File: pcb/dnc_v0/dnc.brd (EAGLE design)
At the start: 100 x 80 mm, 1 part

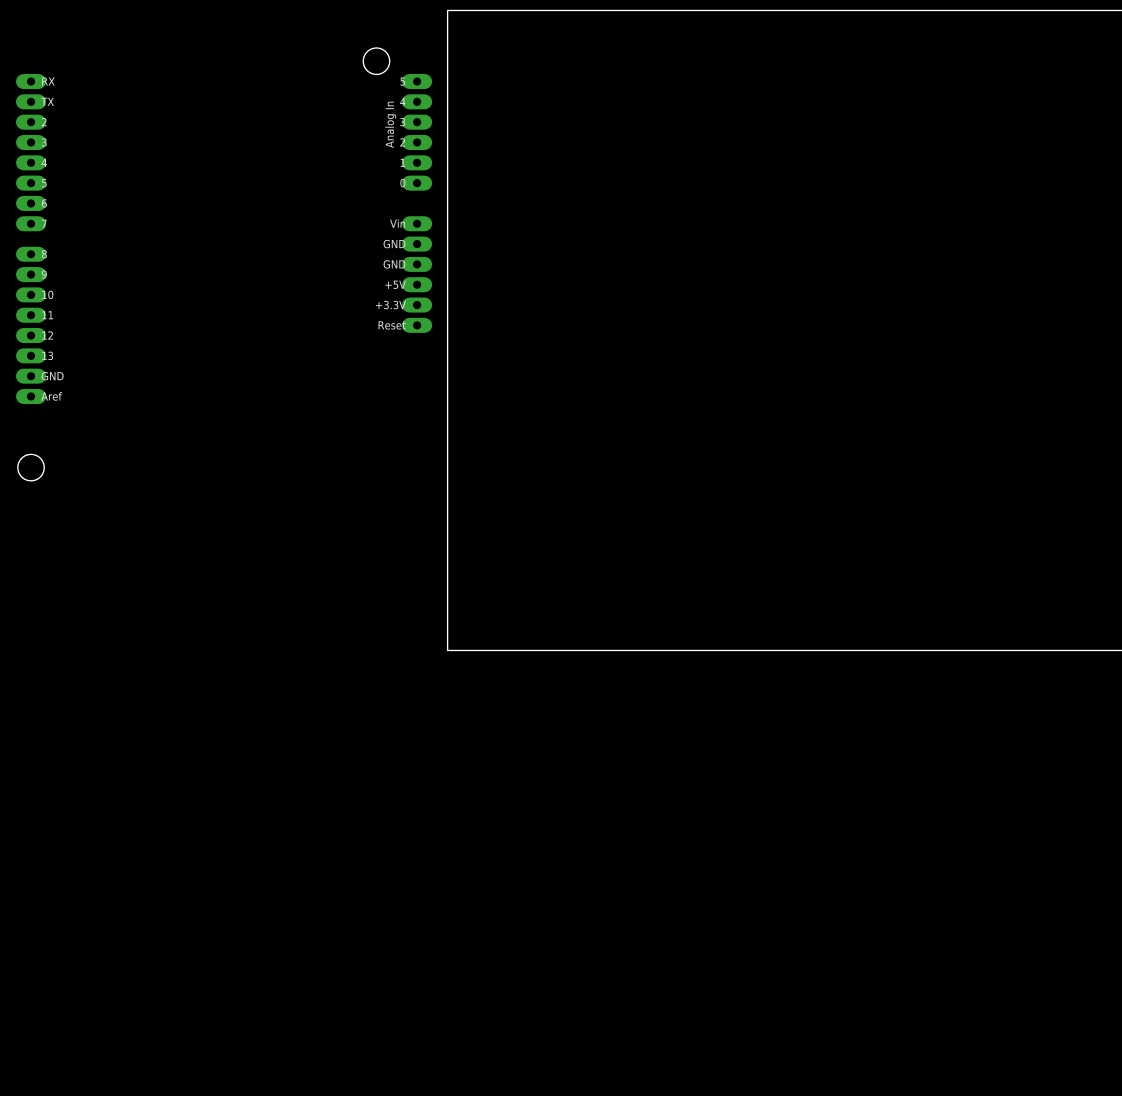
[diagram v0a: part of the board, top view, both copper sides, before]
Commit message: draw yunshield eagle-objet in a eaglelib pcb add sunshield eagle file in docref
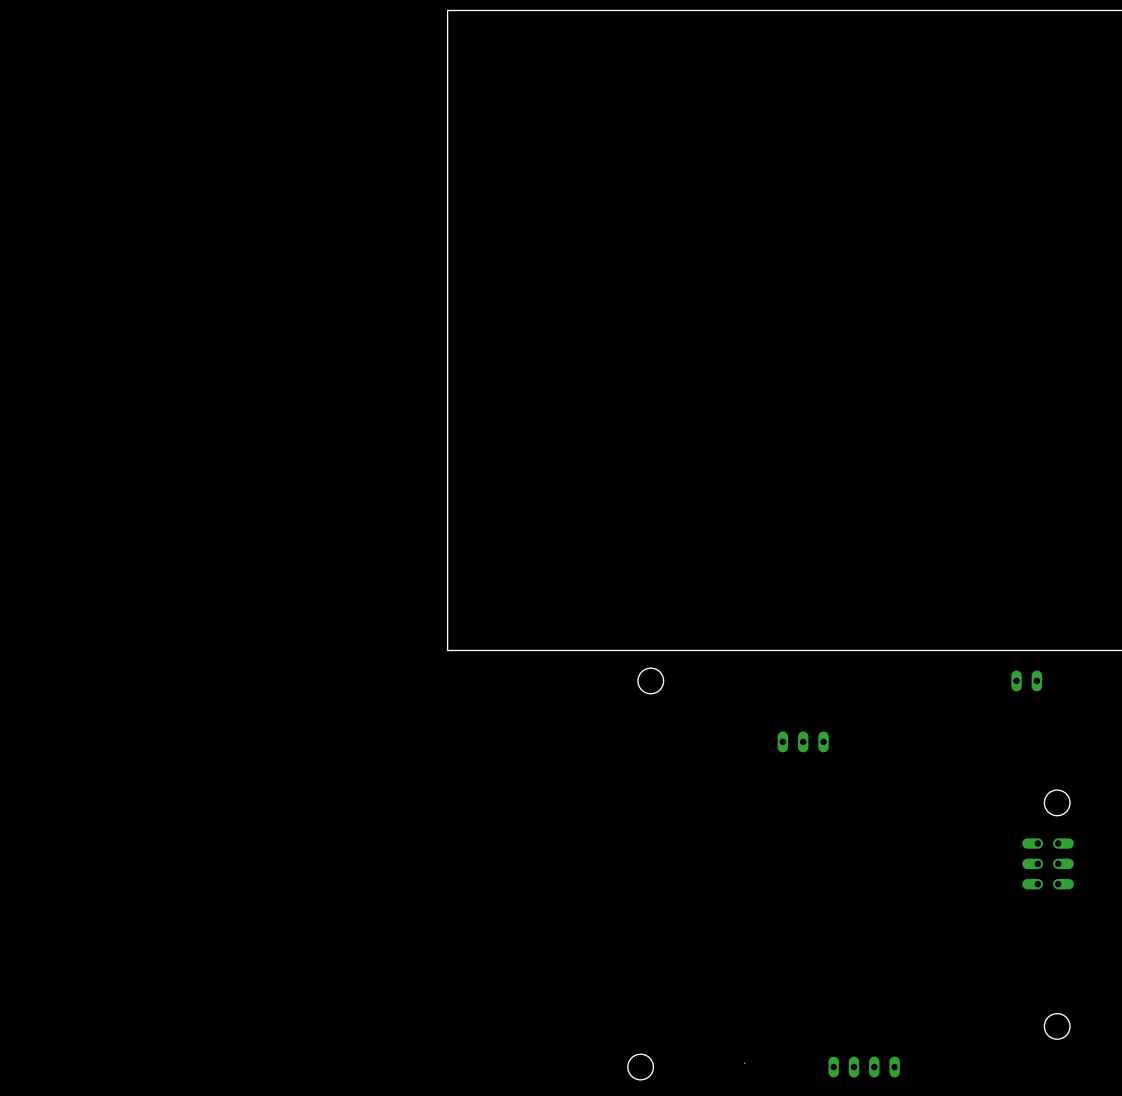
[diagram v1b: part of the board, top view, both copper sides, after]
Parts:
- removed TO_YUN: ARDUINO_SHIELDLONGPADS, SparkFun-Boards:DUEMILANOVE_SHIELD_LONGPADS
- added U$1: YUNBOARD_CONNECT, pierre_vv:YUN-RECEIVE
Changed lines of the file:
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@@
 <setting verticaltext="up"/>
 </settings>
-<grid distance="0.05" unitdist="inch" unit="inch" style="lines" multiple="1" display="no" altdistance="0.025" altunitdist="inch" altunit="inch"/>
+<grid distance="0.05" unitdist="inch" unit="inch" style="lines" multiple="1" display="yes" altdistance="0.025" altunitdist="inch" altunit="inch"/>
 <layers>
 <layer number="1" name="Top" color="4" fill="1" visible="yes" active="yes"/>
@@
 <layer number="27" name="tValues" color="7" fill="1" visible="yes" active="yes"/>
 <layer number="28" name="bValues" color="7" fill="1" visible="yes" active="yes"/>
-<layer number="29" name="tStop" color="7" fill="3" visible="no" active="yes"/>
-<layer number="30" name="bStop" color="7" fill="6" visible="no" active="yes"/>
-<layer number="31" name="tCream" color="7" fill="4" visible="no" active="yes"/>
-<layer number="32" name="bCream" color="7" fill="5" visible="no" active="yes"/>
+<layer number="29" name="tStop" color="7" fill="3" visible="yes" active="yes"/>
+<layer number="30" name="bStop" color="7" fill="6" visible="yes" active="yes"/>
+<layer number="31" name="tCream" color="7" fill="4" visible="yes" active="yes"/>
+<layer number="32" name="bCream" color="7" fill="5" visible="yes" active="yes"/>
 <layer number="33" name="tFinish" color="6" fill="3" visible="no" active="yes"/>
 <layer number="34" name="bFinish" color="6" fill="6" visible="no" active="yes"/>
@@
 <layer number="45" name="Holes" color="7" fill="1" visible="no" active="yes"/>
 <layer number="46" name="Milling" color="3" fill="1" visible="no" active="yes"/>
-<layer number="47" name="Measures" color="7" fill="1" visible="no" active="yes"/>
+<layer number="47" name="Measures" color="7" fill="1" visible="yes" active="yes"/>
 <layer number="48" name="Document" color="7" fill="1" visible="yes" active="yes"/>
 <layer number="49" name="Reference" color="7" fill="1" visible="yes" active="yes"/>
@@
 <layer number="54" name="bGND_GNDA" color="1" fill="9" visible="no" active="no"/>
 <layer number="56" name="wert" color="7" fill="1" visible="no" active="no"/>
+<layer number="57" name="tCAD" color="7" fill="1" visible="no" active="no"/>
 <layer number="90" name="Modules" color="5" fill="1" visible="no" active="no"/>
 <layer number="91" name="Nets" color="2" fill="1" visible="no" active="no"/>
@@
 <layer number="106" name="bPlate" color="7" fill="1" visible="yes" active="yes"/>
 <layer number="107" name="Crop" color="7" fill="1" visible="yes" active="yes"/>
+<layer number="108" name="fp8" color="7" fill="1" visible="no" active="yes"/>
+<layer number="109" name="fp9" color="7" fill="1" visible="no" active="yes"/>
+<layer number="110" name="fp0" color="7" fill="1" visible="no" active="yes"/>
+<layer number="111" name="111" color="7" fill="1" visible="no" active="yes"/>
+<layer number="112" name="tSilk" color="7" fill="1" visible="no" active="yes"/>
 <layer number="116" name="Patch_BOT" color="9" fill="4" visible="yes" active="yes"/>
+<layer number="118" name="Rect_Pads" color="7" fill="1" visible="no" active="yes"/>
 <layer number="121" name="_tsilk" color="7" fill="1" visible="yes" active="yes"/>
 <layer number="122" name="_bsilk" color="7" fill="1" visible="yes" active="yes"/>
+<layer number="123" name="tTestmark" color="7" fill="1" visible="no" active="yes"/>
+<layer number="124" name="bTestmark" color="7" fill="1" visible="no" active="yes"/>
 <layer number="125" name="_tNames" color="7" fill="1" visible="yes" active="yes"/>
+<layer number="126" name="_bNames" color="7" fill="1" visible="no" active="yes"/>
+<layer number="127" name="_tValues" color="7" fill="1" visible="no" active="yes"/>
+<layer number="128" name="_bValues" color="7" fill="1" visible="no" active="yes"/>
+<layer number="131" name="tAdjust" color="7" fill="1" visible="no" active="yes"/>
+<layer number="132" name="bAdjust" color="7" fill="1" visible="no" active="yes"/>
 <layer number="144" name="Drill_legend" color="7" fill="1" visible="yes" active="yes"/>
+<layer number="150" name="Notes" color="7" fill="1" visible="no" active="yes"/>
 <layer number="151" name="HeatSink" color="7" fill="1" visible="yes" active="yes"/>
+<layer number="152" name="_bDocu" color="7" fill="1" visible="no" active="yes"/>
+<layer number="153" name="FabDoc1" color="7" fill="1" visible="no" active="yes"/>
+<layer number="154" name="FabDoc2" color="7" fill="1" visible="no" active="yes"/>
+<layer number="155" name="FabDoc3" color="7" fill="1" visible="no" active="yes"/>
+<layer number="199" name="Contour" color="7" fill="1" visible="no" active="yes"/>
 <layer number="200" name="200bmp" color="1" fill="10" visible="yes" active="yes"/>
 <layer number="201" name="201bmp" color="2" fill="10" visible="yes" active="yes"/>
@@
 <layer number="223" name="223bmp" color="24" fill="1" visible="no" active="no"/>
 <layer number="224" name="224bmp" color="25" fill="1" visible="no" active="no"/>
+<layer number="248" name="Housing" color="7" fill="1" visible="no" active="yes"/>
+<layer number="249" name="Edge" color="7" fill="1" visible="no" active="yes"/>
 <layer number="250" name="Descript" color="3" fill="1" visible="no" active="no"/>
 <layer number="251" name="SMDround" color="12" fill="11" visible="no" active="no"/>
@@
 </autorouter>
 <elements>
-<element name="TO_YUN" library="SparkFun-Boards" package="DUEMILANOVE_SHIELD_LONGPADS" value="ARDUINO_SHIELDLONGPADS" x="-54.61" y="16.51"/>
+<element name="U$1" library="pierre_vv" package="YUN-RECEIVE" value="YUNBOARD_CONNECT" x="48.26" y="-24.13"/>
 </elements>
 <signals>
